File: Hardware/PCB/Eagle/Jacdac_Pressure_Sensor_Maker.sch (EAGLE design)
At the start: 30 parts, among them J1 JACDAC-CONNECTOR, J2 SWD-ADAPTER-, J3 HEADER_MALE-1X07, U1 NCP114ASN330T1G, U2 STM32F042F6P6, U3 BAT54S,235, U4 LPS33HWTR

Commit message: Updated PCB files
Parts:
- removed LABEL1: MMC-LOGO-SM, MMC Eagle:MMC-LOGO-SM
- added C5: 33pF, milador_SMD:CAP_CERAMIC-0805-MP
- C1, C4: value 33pF -> 1uF; device milador_SMD:CAP_CERAMIC-0603 -> milador_SMD:CAP_CERAMIC-0805-MP
- C2: value 1uF -> 33pF; device milador_SMD:CAP_CERAMIC-0603-NO -> milador_SMD:CAP_CERAMIC-0805-MP
- C3: value 1uF -> 0.1uF; device milador_SMD:CAP_CERAMIC-0603-NO -> milador_SMD:CAP_CERAMIC-0805-MP
- D2, D3: value STS521050BL90 -> RCLAMP0521PATCT; device milador_SMD:DIODESOD-523 -> milador_SMD:DIODE-ZENER-AA-STS521050BL90
- R1, R2, R3, R4, R5, R6: device milador_SMD:RESISTOR-0603 -> milador_SMD:RESISTOR-0805-MP
- SJ1, SJ2: device milador_SMD:SOLDERJUMPEROPENED -> milador_SMD:SOLDERJUMPERCLOSED
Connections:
- net +3V3: now also C5.1
- net GND: now also C5.2
- net N$17: now also D3.A2; no longer D3.C
- net N$4: now also C2.1; no longer C1.1
- net N$6: now also R6.1; no longer R5.1
- net N$7: now also R5.1; no longer R6.1
- net VCC: now also C1.1, D2.A2; no longer C2.1, D2.C
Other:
- moved on the sheet: C1, C2, C3, C4, R5, R6

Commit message: Updated design
Use I2C instead of SPI
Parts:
- added U$3: MMC-LOGO-SM, MMC Eagle:MMC-LOGO-SM
- J1: value JACDAC-CONNECTOR -> JACDAC_EDGE_CONN-INNIE; device milador:JACDAC-CONNECTOR -> Jacdac:JACDAC_EDGE_CONN-INNIE
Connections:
- removed net N$17: D3.A2, FB1.2, J1.JDF
- removed net SCK: J3.3, SJ1.1, U2.PA5, U4.SCL/SPC
- new net J_DATA: D3.A2, FB1.2, J1.1
- new net SCL: J3.3, SJ1.1, U2.PA11, U4.SCL/SPC
- net GND: now also J1.2; no longer J1.GND
- net SDA: now also U2.PA12; no longer U2.PA7
- net VCC: now also J1.3; no longer J1.JD5V

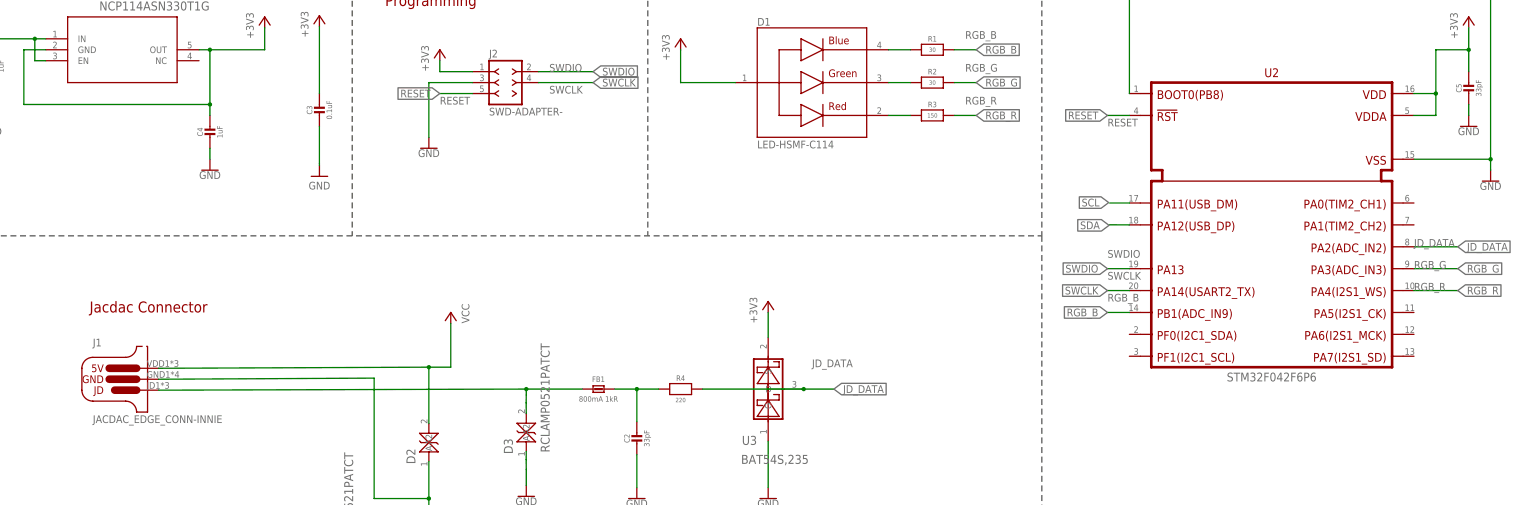
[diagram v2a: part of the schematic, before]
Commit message: Corrected Capacitor values
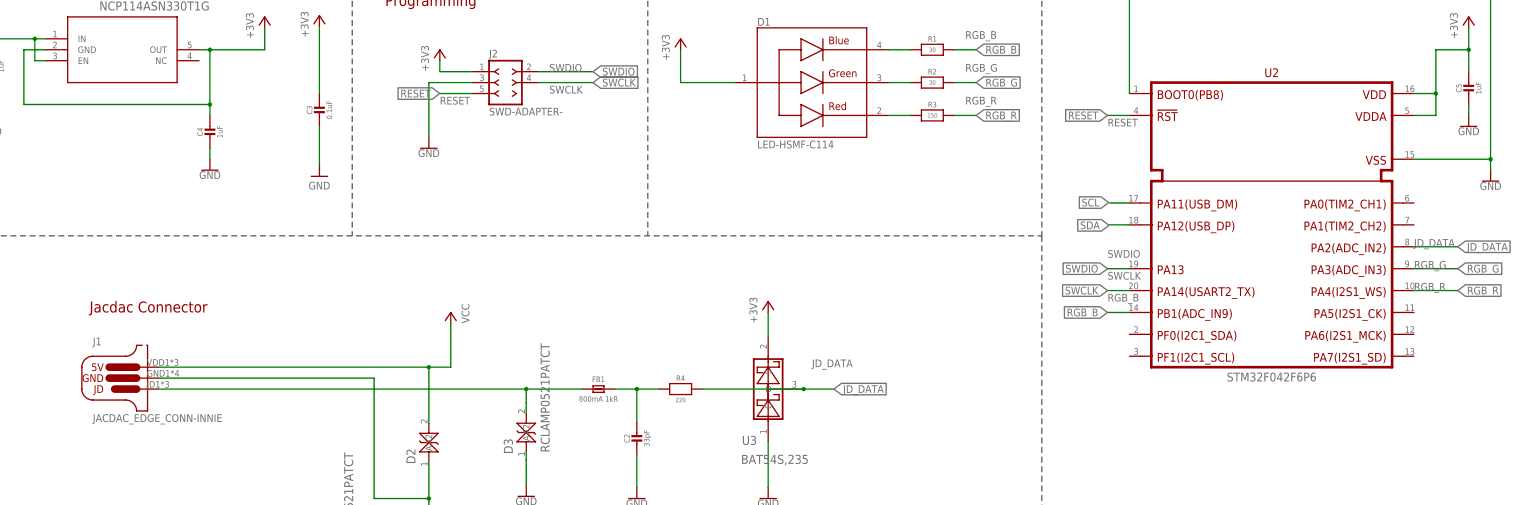
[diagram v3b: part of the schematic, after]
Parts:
- C5: value 33pF -> 1uF
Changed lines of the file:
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@@
 <part name="FRAME1" library="frames" library_urn="urn:adsk.eagle:library:229" deviceset="A3L-LOC" device=""/>
 <part name="+3V5" library="supply1" library_urn="urn:adsk.eagle:library:371" deviceset="+3V3" device=""/>
-<part name="C5" library="milador_SMD" library_urn="urn:adsk.eagle:library:27847482" deviceset="CAP_CERAMIC-" device="0805-MP" package3d_urn="urn:adsk.eagle:package:27847629/3" value="33pF"/>
+<part name="C5" library="milador_SMD" library_urn="urn:adsk.eagle:library:27847482" deviceset="CAP_CERAMIC-" device="0805-MP" package3d_urn="urn:adsk.eagle:package:27847629/3" value="1uF"/>
 <part name="GND9" library="SparkFun-PowerSymbols" deviceset="GND" device=""/>
 <part name="GND10" library="SparkFun-PowerSymbols" deviceset="GND" device=""/>
@@
 </instance>
 <instance part="U$3" gate="G$1" x="304.8" y="73.4822" smashed="yes"/>
-<instance part="J1" gate="G$1" x="56.642" y="149.606" smashed="yes">
-<attribute name="VALUE" x="46.482" y="134.366" size="1.778" layer="96" font="vector"/>
-<attribute name="NAME" x="46.482" y="152.146" size="1.778" layer="95" font="vector"/>
+<instance part="J1" gate="G$1" x="56.642" y="149.86" smashed="yes">
+<attribute name="VALUE" x="46.482" y="134.62" size="1.778" layer="96" font="vector"/>
+<attribute name="NAME" x="46.482" y="152.4" size="1.778" layer="95" font="vector"/>
 </instance>
 </instances>
@@
 </segment>
 <segment>
-<wire x1="61.722" y1="144.526" x2="111.76" y2="144.78" width="0.1524" layer="91"/>
+<wire x1="61.722" y1="144.78" x2="111.76" y2="144.78" width="0.1524" layer="91"/>
 <wire x1="111.76" y1="144.78" x2="111.76" y2="116.84" width="0.1524" layer="91"/>
 <wire x1="111.76" y1="116.84" x2="124.46" y2="116.84" width="0.1524" layer="91"/>
@@
 <segment>
 <pinref part="P+1" gate="VCC" pin="VCC"/>
-<wire x1="61.722" y1="147.066" x2="124.46" y2="147.32" width="0.1524" layer="91"/>
+<wire x1="61.722" y1="147.32" x2="124.46" y2="147.32" width="0.1524" layer="91"/>
 <wire x1="124.46" y1="147.32" x2="129.54" y2="147.32" width="0.1524" layer="91"/>
 <wire x1="129.54" y1="147.32" x2="129.54" y2="157.48" width="0.1524" layer="91"/>
@@
 <net name="J_DATA" class="0">
 <segment>
-<wire x1="61.722" y1="141.986" x2="147.066" y2="142.24" width="0.1524" layer="91"/>
+<wire x1="61.722" y1="142.24" x2="147.066" y2="142.24" width="0.1524" layer="91"/>
 <pinref part="FB1" gate="G$1" pin="2"/>
 <wire x1="147.066" y1="142.24" x2="160.02" y2="142.24" width="0.1524" layer="91"/>

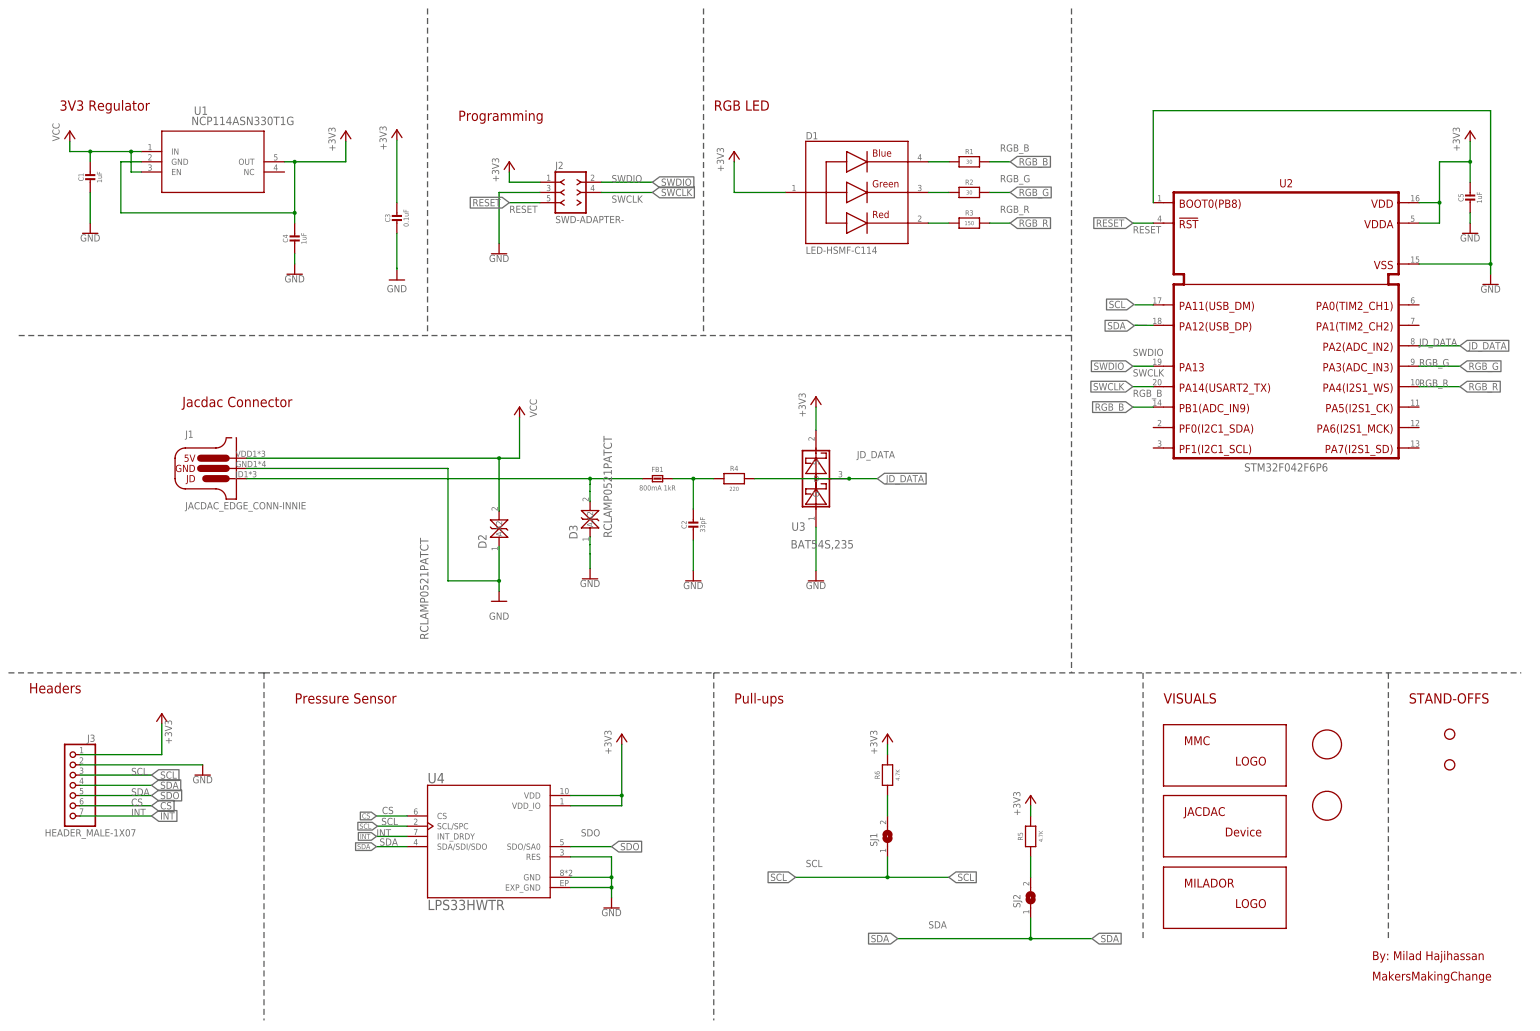
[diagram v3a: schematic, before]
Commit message: Updated design : Centered Pressure Sensor
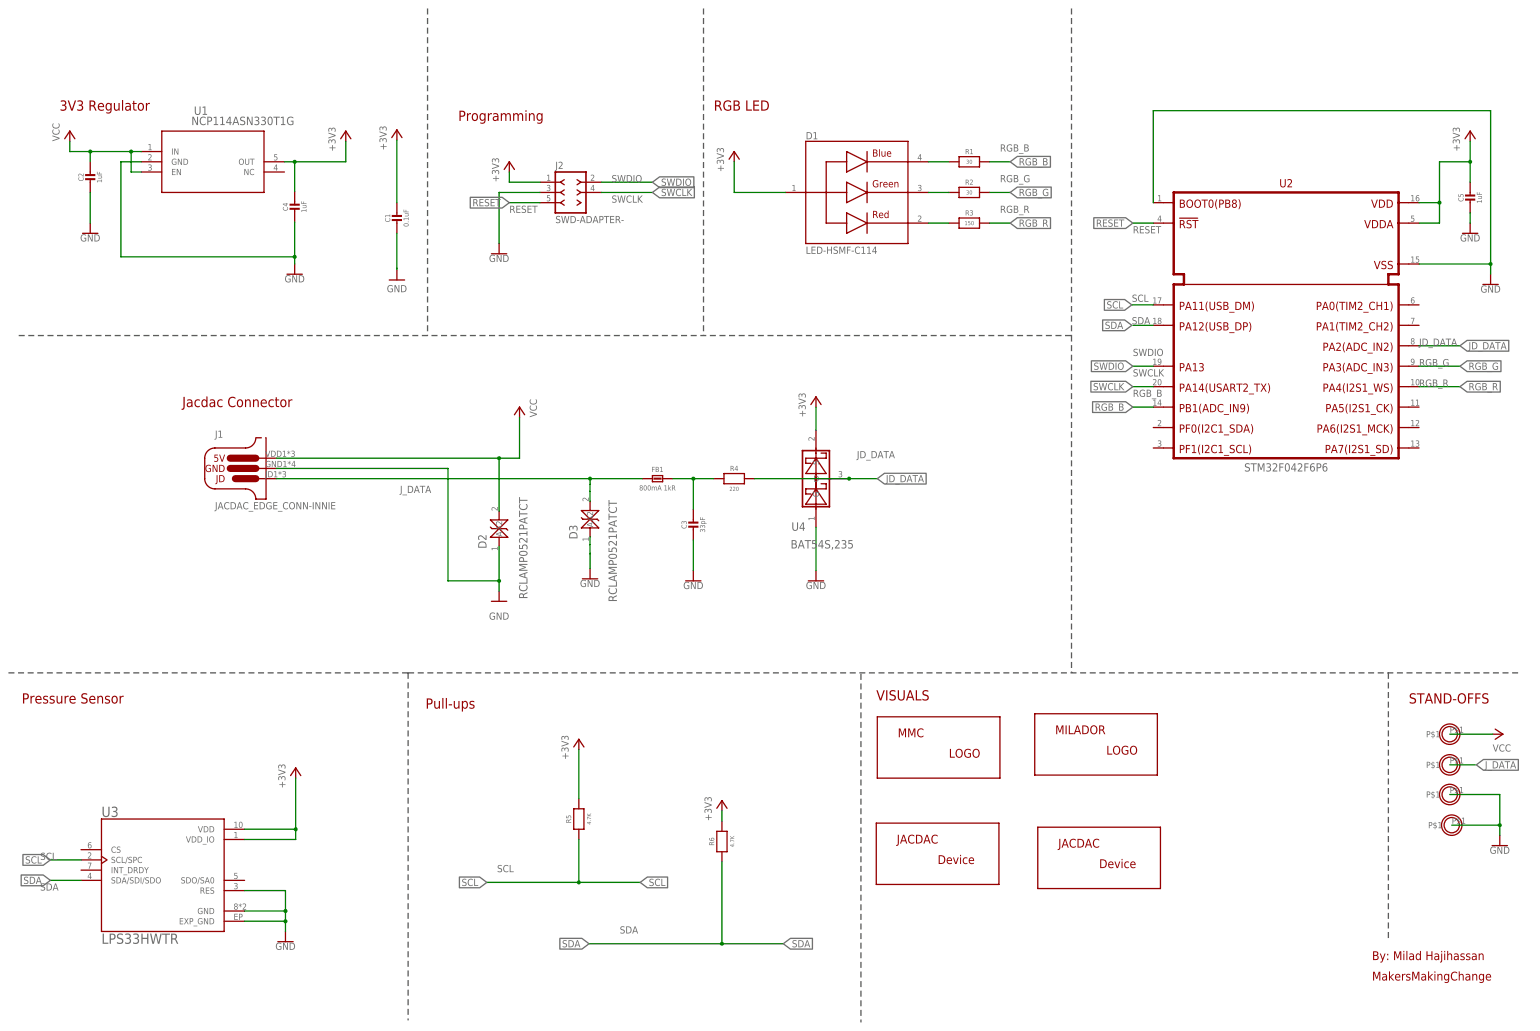
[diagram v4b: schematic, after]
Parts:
- removed J3: HEADER_MALE-1X07, milador:HEADER_MALE-1X07
- removed JP3: STAND-OFF-3.0, milador:STAND-OFF-3.0
- removed SJ1, SJ2: (no value), milador_SMD:SOLDERJUMPERCLOSED
- removed U$2: MILADOR-PIN-NAME-SCK, milador:MILADOR-PIN-NAME-SCK
- removed U$3: MMC-LOGO-SM, MMC Eagle:MMC-LOGO-SM
- added H1, H3, H4: MOUNTINGHOLE2.5, milador:MOUNTINGHOLE2.5
- added MMC_LOGO: MMC_LOGO-SM, MMC Eagle:MMC_LOGO-SM
- C1: value 1uF -> 0.1uF; device milador_SMD:CAP_CERAMIC-0805-MP -> milador_SMD:CAP_CERAMIC-0603-NO
- C2: value 33pF -> 1uF; device milador_SMD:CAP_CERAMIC-0805-MP -> milador_SMD:CAP_CERAMIC-0603-NO
- C3: value 0.1uF -> 33pF; device milador_SMD:CAP_CERAMIC-0805-MP -> milador_SMD:CAP_CERAMIC-0603
- C4: device milador_SMD:CAP_CERAMIC-0805-MP -> milador_SMD:CAP_CERAMIC-0603-NO
- C5: device milador_SMD:CAP_CERAMIC-0805-MP -> milador_SMD:CAP_CERAMIC-0603
- D2, D3: device milador_SMD:DIODE-ZENER-AA-STS521050BL90 -> milador_SMD:DIODE-ZENER-STS521050BL90
- H2: value STAND-OFF-3.0 -> MOUNTINGHOLE2.5; device milador:STAND-OFF-3.0 -> milador:MOUNTINGHOLE2.5
- R1, R2, R3, R4, R5, R6: device milador_SMD:RESISTOR-0805-MP -> milador_SMD:RESISTOR-0603
- U$1: value MILADOR-PIN-NAME-SDA -> JACDAC-DEVICE-LPS33HW; device milador:MILADOR-PIN-NAME-SDA -> milador:JACDAC-DEVICE-LPS33HW
- U3: value BAT54S,235 -> LPS33HWTR; device milador_SMD:BAT54S,235 -> milador_SMD:LPS33HWTR
- U4: value LPS33HWTR -> BAT54S,235; device milador_SMD:LPS33HWTR -> milador_SMD:BAT54S,235
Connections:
- removed net CS: J3.6, U4.CS
- removed net INT: J3.7, U4.INT_DRDY
- removed net N$6: R6.1, SJ1.2
- removed net N$7: R5.1, SJ2.2
- removed net SDO: J3.5, U4.SDO/SA0
- net +3V3: now also C1.1, U3.VDD, U3.VDD_IO, U4.S; no longer C3.1, J3.1, U1.GND, U3.S, U4.VDD, U4.VDD_IO
- net GND: now also H3.P$1, H4.P$1, U1.GND, U3.EXP_GND, U3.GND, U3.RES, U4.G; no longer J3.2, U3.G, U4.EXP_GND, U4.GND, U4.RES
- net JD_DATA: now also U4.D; no longer U3.D
- net J_DATA: now also H2.P$1
- net N$4: now also C3.1; no longer C2.1
- net SCL: now also R5.1, U3.SCL/SPC; no longer J3.3, SJ1.1, U4.SCL/SPC
- net SDA: now also R6.1, U3.SDA/SDI/SDO; no longer J3.4, SJ2.1, U4.SDA/SDI/SDO
- net VCC: now also C2.1, H1.P$1; no longer C1.1
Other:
- note removed: "Headers"
- moved on the sheet: C1, C2, C3, C4, J1, R5, R6

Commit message: Added version 1.0
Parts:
- removed D2, D3: RCLAMP0521PATCT, milador_SMD:DIODE-ZENER-STS521050BL90
- removed H1, H2, H3, H4: MOUNTINGHOLE2.5, milador:MOUNTINGHOLE2.5
- removed J1: JACDAC_EDGE_CONN-INNIE, Jacdac:JACDAC_EDGE_CONN-INNIE
- removed LABEL2: JACDAC-DEVICE-PS, milador:JACDAC-DEVICE-PS
- removed U$1: JACDAC-DEVICE-LPS33HW, milador:JACDAC-DEVICE-LPS33HW
- added J3: 5V, milador:JACDAC-M3-PWR-OUTL
- added J4: DATA, milador:JACDAC-M3-DATA-NOTCH
- added J5, J6: GND, milador:JACDAC-M3-GND
- added JD1, JD2: JACDAC-EDGE-OUTIE, milador:JACDAC-EDGE-OUTIE
- added LABEL_JACDAC_PS: MILADOR-JACDAC-DEVICE-PS, milador:MILADOR-JACDAC-DEVICE-PS
- added LABEL_LPS33HW: MILADOR-JACDAC-DEVICE-LPS33HW, milador:MILADOR-JACDAC-DEVICE-LPS33HW
- added LABEL_QR_CODE: MILADOR-QR-CODE-JACDAC-GITHUB-PS, milador:MILADOR-QR-CODE-JACDAC-GITHUB-PS
- C1: value 0.1uF -> 1uF
- C2: value 1uF -> 33pF; device milador_SMD:CAP_CERAMIC-0603-NO -> milador_SMD:CAP_CERAMIC-0603
- C3: value 33pF -> 1uF; device milador_SMD:CAP_CERAMIC-0603 -> milador_SMD:CAP_CERAMIC-0603-NO
- C4: value 1uF -> 0.1uF
- MMC_LOGO: value MMC_LOGO-SM -> MMC_LOGO-XSM; device MMC Eagle:MMC_LOGO-SM -> MMC Eagle:MMC_LOGO-XSM
- U1: value NCP114ASN330T1G -> STM32F042F6P6; device milador_SMD:NCP114ASN330T1G -> milador_SMD:STM32F042F6P6
- U2: value STM32F042F6P6 -> NCP114ASN330T1G; device milador_SMD:STM32F042F6P6 -> milador_SMD:NCP114ASN330T1G
- renumbered LABEL3 to LABEL_MILADOR
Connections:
- net +3V3: now also C3.1, U1.VDD, U1.VDDA, U2.OUT; no longer C1.1, U1.OUT, U2.VDD, U2.VDDA
- net GND: now also J5.P$1, J6.P$1, JD1.1, JD2.1, U1.BOOT0, U1.VSS, U2.GND; no longer D2.A, D3.A, H3.P$1, H4.P$1, J1.2, U1.GND, U2.BOOT0, U2.VSS
- net JD_DATA: now also U1.PA2; no longer U2.PA2
- net J_DATA: now also J4.P$1, JD1.2, JD1.6, JD2.2, JD2.6; no longer D3.A2, H2.P$1, J1.1
- net N$4: now also C2.1; no longer C3.1
- net RESET: now also U1.!RST; no longer U2.!RST
- net RGB_B: now also U1.PB1; no longer U2.PB1
- net RGB_G: now also U1.PA4; no longer U2.PA3
- net RGB_R: now also U1.PA3; no longer U2.PA4
- net SCL: now also U1.PA11; no longer U2.PA11
- net SDA: now also U1.PA12; no longer U2.PA12
- net SWCLK: now also U1.PA14; no longer U2.PA14
- net SWDIO: now also U1.PA13; no longer U2.PA13
- net VCC: now also C1.1, J3.P$1, JD1.3, JD1.4, JD2.3, JD2.4, U2.EN, U2.IN; no longer C2.1, D2.A2, H1.P$1, J1.3, U1.EN, U1.IN
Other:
- note added: "Jacdac Connector 2"
- note added: "STM32F042F6P6"
- note removed: "MakersMakingChange"
- moved on the sheet: C1, C2, C3, C4, FB1, R4, U4
